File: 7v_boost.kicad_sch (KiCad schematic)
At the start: 5 parts, among them U401 LM27313XMFX/NOPB

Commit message: Update 7v_boost.kicad_sch
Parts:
- added C1401: 330pF 50V, BR_Passives:C_0402_1005Metric, symbol BR_Capacitors_0402:C_0402_330pF_50V_C0G_5%
- added R1401: 13.3k, BR_Passives:C_0402_1005Metric-minimized, symbol BR_Resistors_0402:R_0402_13k3
- added R1402: 62k, BR_Passives:C_0402_1005Metric-minimized, symbol BR_Resistors_0402:R_0402_62k
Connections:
- net GND: now also R1401.2
- net VIN: now reaches C402.1, L401.1, U401.4 (EN), U401.5 (VIN)
- net at D401.2 (A), L401.2, U401.1 (SW): now also C1401.1
- net VOUT: now reaches C401.1
- net VOUT: now also D401.1 (K), C1401.2, R1402.2
- net at U401.3 (FB): now also R1401.1, R1402.1
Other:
- note added: "Iout = 20mA deltaIL = Vin*tON/L = 9.42mA -> ILmax = 24.7mA < Isat"
- note added: "R1401 recommended to be 13.3k R1402 = R1401 * (Vout/1.23 - 1) = 62.3k"
- note added: "Vin = 4V Vout = 7V Vout = Vin/(1-D) -> D = 45.21% (including diode drop) -> tON = 283ns"
- moved on the sheet: C401, C402, D401, L401, U401

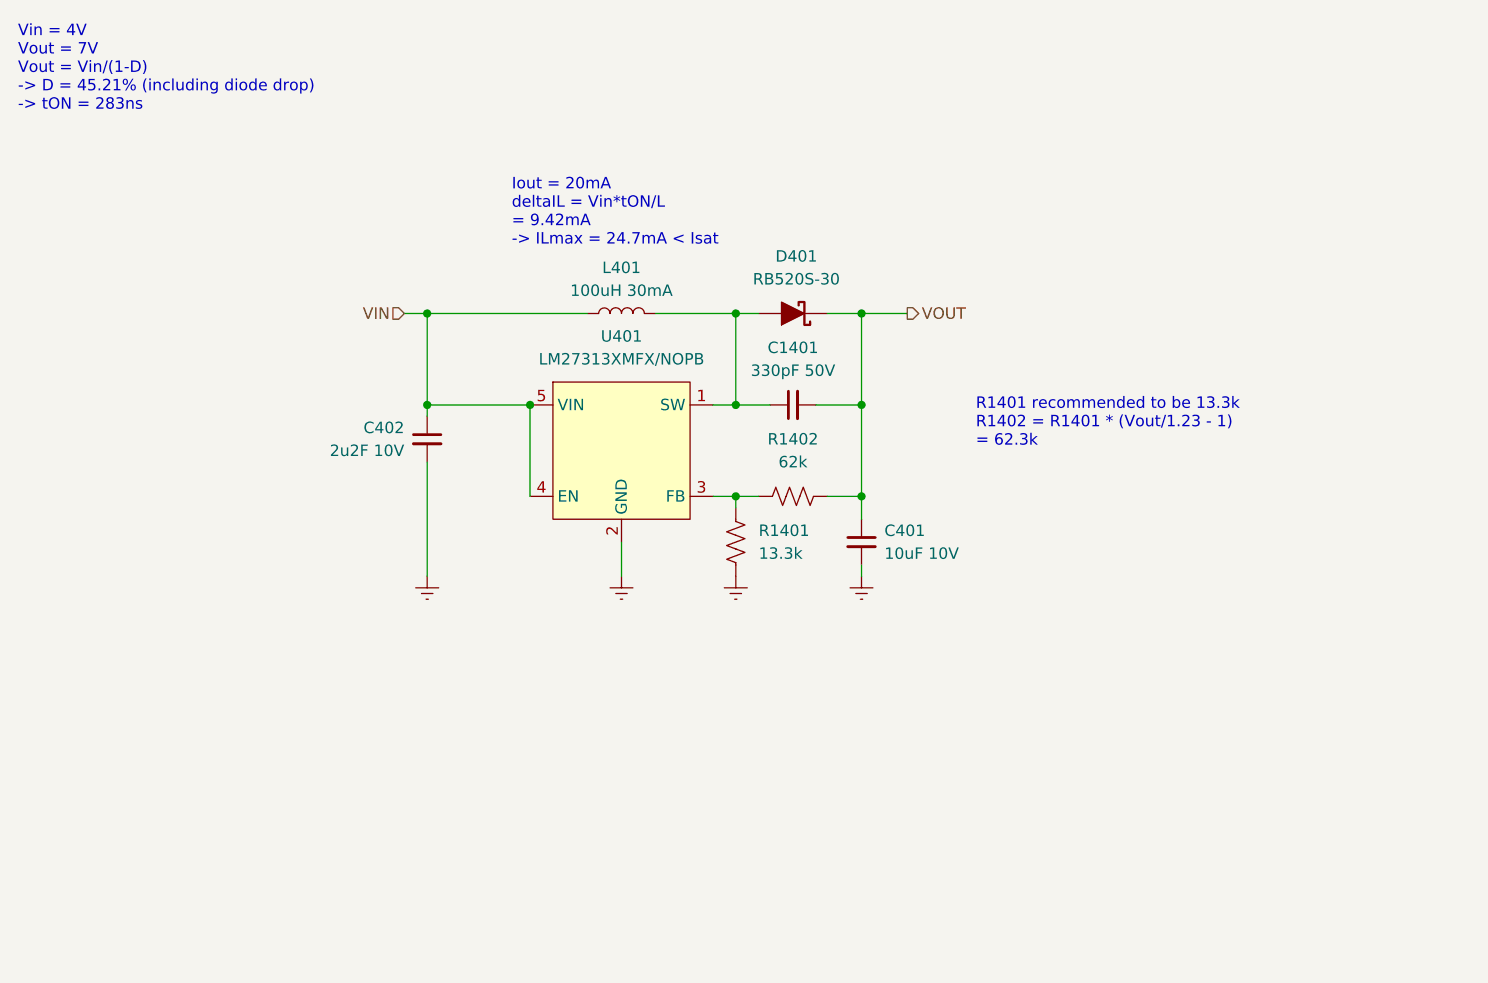
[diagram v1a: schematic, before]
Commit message: finished modifying vcc for sonar + 7V boost updates
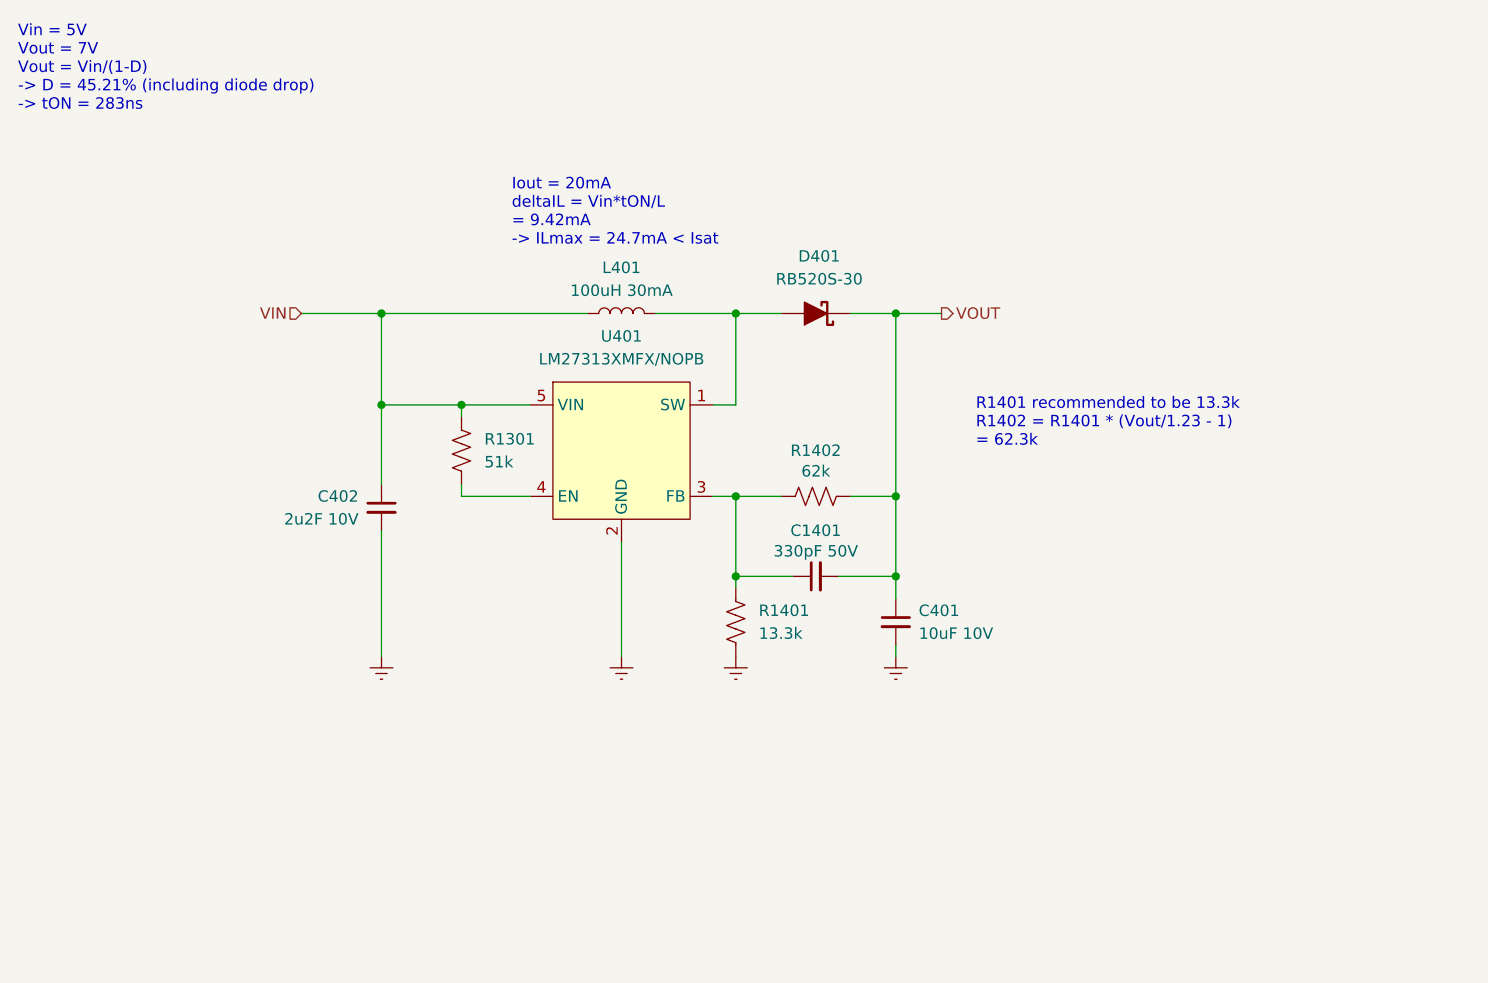
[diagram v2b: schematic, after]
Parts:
- added R1301: 51k, BR_Passives:C_0402_1005Metric-minimized, symbol BR_Resistors_0402:R_0402_51k
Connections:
- net VIN: now also R1301.1; no longer U401.4 (EN)
- net at D401.2 (A), L401.2, U401.1 (SW): no longer C1401.1
- net at R1401.1, R1402.1, U401.3 (FB): now also C1401.1
- new net: R1301.2, U401.4 (EN)
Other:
- note added: "Vin = 5V Vout = 7V Vout = Vin/(1-D) -> D = 45.21% (including diode drop) -> tON = 283ns"
- note removed: "Vin = 4V Vout = 7V Vout = Vin/(1-D) -> D = 45.21% (including diode drop) -> tON = 283ns"
- moved on the sheet: C1401, C401, C402, D401, R1401, R1402

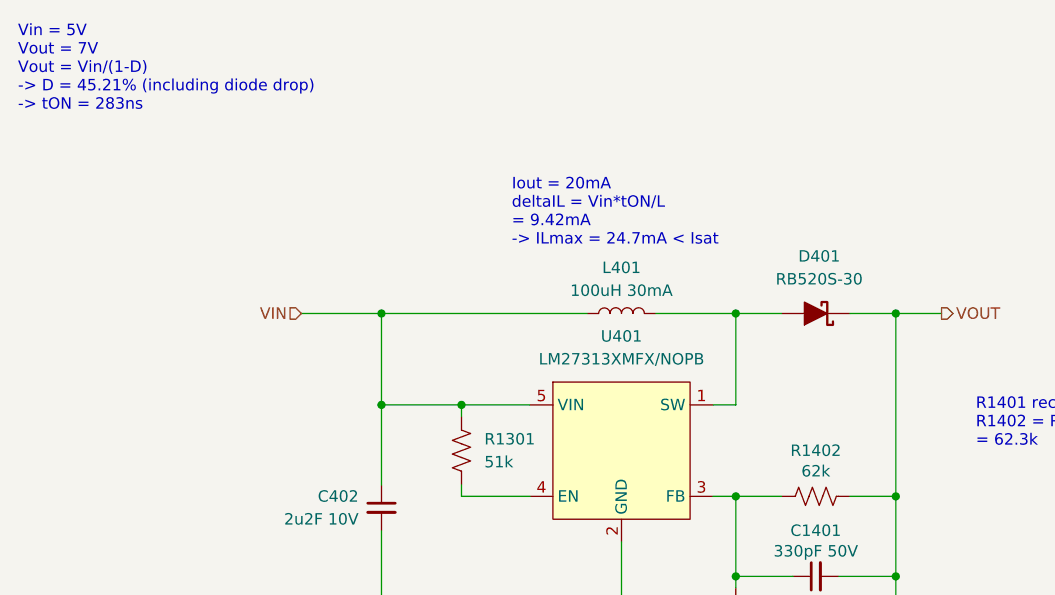
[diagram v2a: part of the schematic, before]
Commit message: implementing feedback + added stepper driver
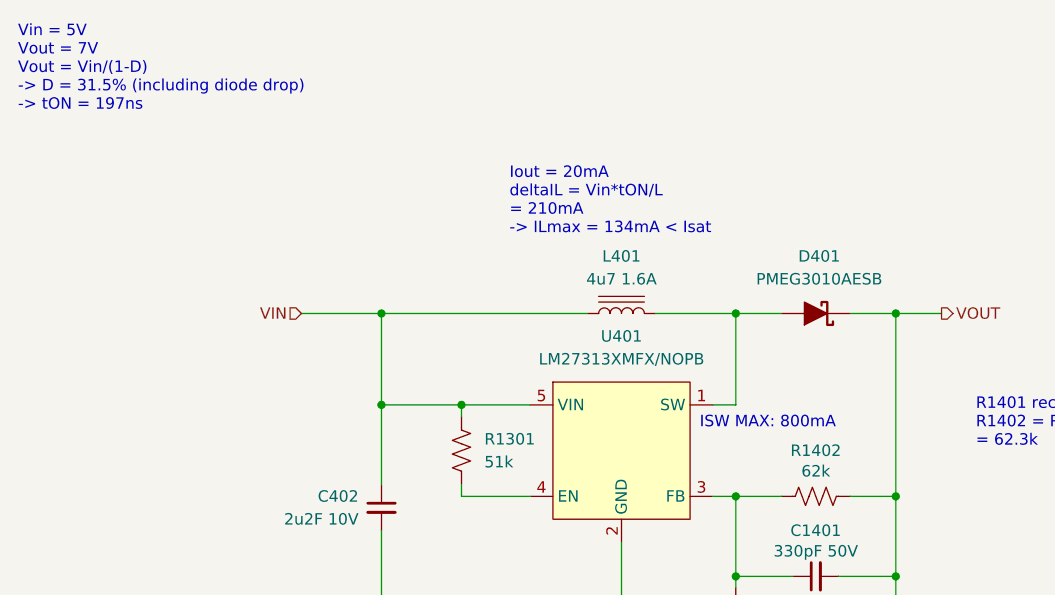
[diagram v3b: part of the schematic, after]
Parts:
- D401: value RB520S-30 -> PMEG3010AESB; footprint BR_Discretes:D_SOD-523 -> BR_Discretes:D_SOD-993-minimized; symbol BR_Diodes:D_Schottky_RB520S-30 -> BR_Diodes:D_Schottky_PMEG3010AESB; BRE Number BRE-000122 -> BRE-000120; JLCPCB Part Num C511880 -> C28646369; Manufacturer onsemi -> Nexperia; Manufacturer Part Num RB520S30T5G -> PMEG3010AESBYL; Supplier Part Num 1 RB520S30T5GOSCT-ND -> 1727-2401-2-ND; Supplier Part Num 2 863-RB520S30T5G -> 771-PMEG3010AESBYL; Supplier Part Num 3 C511880 -> C28646369
- L401: value 100uH 30mA -> 4u7 1.6A; footprint BR_Inductors:LMSC20120652R2MTA -> BR_Inductors:L_1008_2520Metric; symbol BR_Inductors:L_MLZ2012N101LT000 -> BR_Inductors:L_AWP_252012FW-4R7M; BRE Number BRE-001234 -> BRE-000220; JLCPCB Part Num C88184 -> C17225812; Manufacturer TDK -> TAI-TECH Advanced Electronics Co., Ltd.; Manufacturer Part Num MLZ2012N101LT000 -> AWP 252012FW-4R7M; Supplier 1 (none) -> DigiKey; Supplier 2 (none) -> DigiKey; Supplier 3 (none) -> JLCPCB; Supplier Part Num 1 (none) -> 4816-AWP252012FW-4R7MCT-ND; Supplier Part Num 2 (none) -> 4816-AWP252012FW-4R7MTR-ND; Supplier Part Num 3 (none) -> C17225812
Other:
- note added: "ISW MAX: 800mA"
- note added: "Iout = 20mA deltaIL = Vin*tON/L = 210mA -> ILmax = 134mA < Isat"
- note added: "Vin = 5V Vout = 7V Vout = Vin/(1-D) -> D = 31.5% (including diode drop) -> tON = 197ns"
- note removed: "Iout = 20mA deltaIL = Vin*tON/L = 9.42mA -> ILmax = 24.7mA < Isat"
- note removed: "Vin = 5V Vout = 7V Vout = Vin/(1-D) -> D = 45.21% (including diode drop) -> tON = 283ns"
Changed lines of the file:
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@@
 	(generator_version "9.0")
 	(paper "A5")
-	(text "Iout = 20mA\ndeltaIL = Vin*tON/L\n= 9.42mA\n-> ILmax = 24.7mA < Isat"
+	(text "ISW MAX: 800mA"
 		(exclude_from_sim no)
-		(at 83.058 38.354 0)
+		(at 111.506 61.722 0)
+		(effects
+			(font
+				(size 1.27 1.27)
+			)
+		)
+	)
+	(text "Iout = 20mA\ndeltaIL = Vin*tON/L\n= 210mA\n-> ILmax = 134mA < Isat"
+		(exclude_from_sim no)
+		(at 82.804 37.084 0)
 		(effects
 			(font
@@
 		)
 	)
-	(text "Vin = 5V\nVout = 7V\nVout = Vin/(1-D)\n-> D = 45.21% (including diode drop)\n-> tON = 283ns"
+	(text "Vin = 5V\nVout = 7V\nVout = Vin/(1-D)\n-> D = 31.5% (including diode drop)\n-> tON = 197ns"
 		(exclude_from_sim no)
 		(at 28.194 22.352 0)
@@
 	)
 	(symbol
-		(lib_id "BR_Inductors:L_MLZ2012N101LT000")
+		(lib_id "BR_Inductors:L_AWP_252012FW-4R7M")
 		(at 95.25 49.53 90)
 		(unit 1)
@@
 		(fields_autoplaced yes)
 		(property "Reference" "L401"
-			(at 95.25 44.45 90)
-			(effects
-				(font
-					(size 1.27 1.27)
-				)
-			)
-		)
-		(property "Value" "100uH 30mA"
-			(at 95.25 46.99 90)
-			(effects
-				(font
-					(size 1.27 1.27)
-				)
-			)
-		)
-		(property "Footprint" "BR_Inductors:LMSC20120652R2MTA"
+			(at 95.25 43.18 90)
+			(effects
+				(font
+					(size 1.27 1.27)
+				)
+			)
+		)
+		(property "Value" "4u7 1.6A"
+			(at 95.25 45.72 90)
+			(effects
+				(font
+					(size 1.27 1.27)
+				)
+			)
+		)
+		(property "Footprint" "BR_Inductors:L_1008_2520Metric"
 			(at 19.05 49.53 0)
 			(effects
@@
 			)
 		)
-		(property "Datasheet" "https://lcsc.com/datasheet/lcsc_datasheet_2412231059_TDK-MLZ2012N101LT000_C88184.pdf"
+		(property "Datasheet" "https://mm.digikey.com/Volume0/opasdata/d220001/medias/docus/5561/AWP%20Series.pdf"
 			(at 21.59 49.53 0)
 			(effects
@@
 			)
 		)
-		(property "Description" "100uH 20% 30mA 3.5Ω Inductors SMT 0805"
+		(property "Description" "4.7uH 20% 1.6A 175mR Shielded Molded Inductor SMT 1008 package"
 			(at 24.13 49.53 0)
 			(effects
@@
 			)
 		)
-		(property "Manufacturer" "TDK"
+		(property "Manufacturer" "TAI-TECH Advanced Electronics Co., Ltd."
 			(at 26.67 49.53 0)
 			(effects
@@
 			)
 		)
-		(property "Manufacturer Part Num" "MLZ2012N101LT000"
+		(property "Manufacturer Part Num" "AWP 252012FW-4R7M"
 			(at 29.21 49.53 0)
 			(effects
@@
 			)
 		)
-		(property "BRE Number" "BRE-001234"
+		(property "BRE Number" "BRE-000220"
 			(at 31.75 49.53 0)
 			(effects
@@
 			)
 		)
-		(property "JLCPCB Part Num" "C88184"
+		(property "JLCPCB Part Num" "C17225812"
+			(at 49.53 49.53 0)
+			(effects
+				(font
+					(size 1.27 1.27)
+				)
+				(justify left)
+				(hide yes)
+			)
+		)
+		(property "Supplier 1" "DigiKey"
 			(at 34.29 49.53 0)
+			(effects
+				(font
+					(size 1.27 1.27)
+				)
+				(justify left)
+				(hide yes)
+			)
+		)
+		(property "Supplier Part Num 1" "4816-AWP252012FW-4R7MCT-ND"
+			(at 36.83 49.53 0)
+			(effects
+				(font
+					(size 1.27 1.27)
+				)
+				(justify left)
+				(hide yes)
+			)
+		)
+		(property "Supplier 2" "DigiKey"
+			(at 39.37 49.53 0)
+			(effects
+				(font
+					(size 1.27 1.27)
+				)
+				(justify left)
+				(hide yes)
+			)
+		)
+		(property "Supplier Part Num 2" "4816-AWP252012FW-4R7MTR-ND"
+			(at 41.91 49.53 0)
+			(effects
+				(font
+					(size 1.27 1.27)
+				)
+				(justify left)
+				(hide yes)
+			)
+		)
+		(property "Supplier 3" "JLCPCB"
+			(at 44.45 49.53 0)
+			(effects
+				(font
+					(size 1.27 1.27)
+				)
+				(justify left)
+				(hide yes)
+			)
+		)
+		(property "Supplier Part Num 3" "C17225812"
+			(at 46.99 49.53 0)
 			(effects
 				(font
@@
 	)
 	(symbol
-		(lib_id "BR_Diodes:D_Schottky_RB520S-30")
+		(lib_id "BR_Diodes:D_Schottky_PMEG3010AESB")
 		(at 116.84 49.53 180)
 		(unit 1)
@@
 			)
 		)
-		(property "Value" "RB520S-30"
+		(property "Value" "PMEG3010AESB"
 			(at 117.221 45.72 0)
 			(effects
@@
 			)
 		)
-		(property "Footprint" "BR_Discretes:D_SOD-523"
+		(property "Footprint" "BR_Discretes:D_SOD-993-minimized"
 			(at 116.84 125.73 0)
 			(effects
@@
 			)
 		)
-		(property "Datasheet" "https://www.onsemi.com/pdf/datasheet/rb520s30t1-d.pdf"
+		(property "Datasheet" "https://assets.nexperia.com/documents/data-sheet/PMEG3010AESB.pdf"
 			(at 116.84 123.19 0)
 			(effects
@@
 			)
 		)
-		(property "Description" "Schottky Diode 30V 200mA SOD-523"
+		(property "Description" "Schottky Diode 30V 1A SOD-993"
+			(at 116.84 120.65 0)
+			(effects
+				(font
+					(size 1.27 1.27)
+				)
+				(justify left)
+				(hide yes)
+			)
+		)
+		(property "Manufacturer" "Nexperia"
+			(at 116.84 118.11 0)
+			(effects
+				(font
+					(size 1.27 1.27)
+				)
+				(justify left)
+				(hide yes)
+			)
+		)
+		(property "Manufacturer Part Num" "PMEG3010AESBYL"
+			(at 116.84 115.57 0)
+			(effects
+				(font
+					(size 1.27 1.27)
+				)
+				(justify left)
+				(hide yes)
+			)
+		)
+		(property "BRE Number" "BRE-000120"
 			(at 116.84 113.03 0)
-			(effects
-				(font
-					(size 1.27 1.27)
-				)
-				(justify left)
-				(hide yes)
-			)
-		)
-		(property "Manufacturer" "onsemi"
-			(at 116.84 120.65 0)
-			(effects
-				(font
-					(size 1.27 1.27)
-				)
-				(justify left)
-				(hide yes)
-			)
-		)
-		(property "Manufacturer Part Num" "RB520S30T5G"
-			(at 116.84 118.11 0)
-			(effects
-				(font
-					(size 1.27 1.27)
-				)
-				(justify left)
-				(hide yes)
-			)
-		)
-		(property "BRE Number" "BRE-000122"
-			(at 116.84 115.57 0)
 			(effects
 				(font
@@
 			)
 		)
-		(property "Supplier Part Num 1" "RB520S30T5GOSCT-ND"
+		(property "Supplier Part Num 1" "1727-2401-2-ND"
 			(at 116.84 107.95 0)
 			(effects
@@
 			)
 		)
-		(property "Supplier Part Num 2" "863-RB520S30T5G"
+		(property "Supplier Part Num 2" "771-PMEG3010AESBYL"
 			(at 116.84 102.87 0)
 			(effects
@@
 			)
 		)
-		(property "Supplier Part Num 3" "C511880"
+		(property "Supplier Part Num 3" "C28646369"
 			(at 116.84 97.79 0)
 			(effects
@@
 			)
 		)
-		(property "JLCPCB Part Num" "C511880"
-			(at 116.84 90.17 0)
-			(effects
-				(font
+		(property "JLCPCB Part Num" "C28646369"
+			(at 116.84 95.25 0)
+			(effects
+				(font

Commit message: completed feedback from review + reannotated sheets
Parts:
- renumbered C402 to C1301, C1401 to C1302, C401 to C1303, D401 to D1301, L401 to L1301, R1401 to R1302, R1402 to R1303, U401 to U1301
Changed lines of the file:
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@@
 		(dnp no)
 		(fields_autoplaced yes)
-		(property "Reference" "#PWR0403"
+		(property "Reference" "#PWR01302"
 			(at 95.25 93.98 0)
 			(effects
@@
 			(project "SonarDevBoard"
 				(path "/2a5ce3ef-537a-4122-a1be-ef76186bc0d7/774f2c6c-c15c-4713-acf0-4edb2ec6be20/ba770378-fa99-4e9b-ba3e-dcadec87fa26"
-					(reference "#PWR0403")
+					(reference "#PWR01302")
 					(unit 1)
 				)
@@
 		(on_board yes)
 		(dnp no)
-		(property "Reference" "C1401"
+		(property "Reference" "C1302"
 			(at 116.84 73.66 90)
 			(effects
@@
 			(project ""
 				(path "/2a5ce3ef-537a-4122-a1be-ef76186bc0d7/774f2c6c-c15c-4713-acf0-4edb2ec6be20/ba770378-fa99-4e9b-ba3e-dcadec87fa26"
-					(reference "C1401")
+					(reference "C1302")
 					(unit 1)
 				)
@@
 		(on_board yes)
 		(dnp no)
-		(property "Reference" "C402"
+		(property "Reference" "C1301"
 			(at 66.04 69.8562 0)
 			(effects
@@
 			(project "SonarDevBoard"
 				(path "/2a5ce3ef-537a-4122-a1be-ef76186bc0d7/774f2c6c-c15c-4713-acf0-4edb2ec6be20/ba770378-fa99-4e9b-ba3e-dcadec87fa26"
-					(reference "C402")
+					(reference "C1301")
 					(unit 1)
 				)
@@
 		(dnp no)
 		(fields_autoplaced yes)
-		(property "Reference" "L401"
+		(property "Reference" "L1301"
 			(at 95.25 43.18 90)
 			(effects
@@
 			(project "SonarDevBoard"
 				(path "/2a5ce3ef-537a-4122-a1be-ef76186bc0d7/774f2c6c-c15c-4713-acf0-4edb2ec6be20/ba770378-fa99-4e9b-ba3e-dcadec87fa26"
-					(reference "L401")
+					(reference "L1301")
 					(unit 1)
 				)
@@
 		(dnp no)
 		(fields_autoplaced yes)
-		(property "Reference" "R1401"
+		(property "Reference" "R1302"
 			(at 110.49 82.5499 0)
 			(effects
@@
 			(project ""
 				(path "/2a5ce3ef-537a-4122-a1be-ef76186bc0d7/774f2c6c-c15c-4713-acf0-4edb2ec6be20/ba770378-fa99-4e9b-ba3e-dcadec87fa26"
-					(reference "R1401")
+					(reference "R1302")
 					(unit 1)
 				)
@@
 		(dnp no)
 		(fields_autoplaced yes)
-		(property "Reference" "#PWR01401"
+		(property "Reference" "#PWR01303"
 			(at 107.95 93.98 0)
 			(effects
@@
 			(project "SonarDevBoard"
 				(path "/2a5ce3ef-537a-4122-a1be-ef76186bc0d7/774f2c6c-c15c-4713-acf0-4edb2ec6be20/ba770378-fa99-4e9b-ba3e-dcadec87fa26"
-					(reference "#PWR01401")
+					(reference "#PWR01303")
 					(unit 1)
 				)
@@
 		(dnp no)
 		(fields_autoplaced yes)
-		(property "Reference" "C401"
+		(property "Reference" "C1303"
 			(at 128.27 82.5562 0)
 			(effects
@@
 			(project "SonarDevBoard"
 				(path "/2a5ce3ef-537a-4122-a1be-ef76186bc0d7/774f2c6c-c15c-4713-acf0-4edb2ec6be20/ba770378-fa99-4e9b-ba3e-dcadec87fa26"
-					(reference "C401")
+					(reference "C1303")
 					(unit 1)
 				)
@@
 		(dnp no)
 		(fields_autoplaced yes)
-		(property "Reference" "D401"
+		(property "Reference" "D1301"
 			(at 117.221 43.18 0)
 			(effects
@@
 			(project "SonarDevBoard"
 				(path "/2a5ce3ef-537a-4122-a1be-ef76186bc0d7/774f2c6c-c15c-4713-acf0-4edb2ec6be20/ba770378-fa99-4e9b-ba3e-dcadec87fa26"
-					(reference "D401")
+					(reference "D1301")
 					(unit 1)
 				)
@@
 		(on_board yes)
 		(dnp no)
-		(property "Reference" "R1402"
+		(property "Reference" "R1303"
 			(at 116.84 64.77 90)
 			(effects
@@
 			(project ""
 				(path "/2a5ce3ef-537a-4122-a1be-ef76186bc0d7/774f2c6c-c15c-4713-acf0-4edb2ec6be20/ba770378-fa99-4e9b-ba3e-dcadec87fa26"
-					(reference "R1402")
+					(reference "R1303")
 					(unit 1)
 				)
@@
 		(dnp no)
 		(fields_autoplaced yes)
-		(property "Reference" "#PWR0402"
+		(property "Reference" "#PWR01304"
 			(at 125.73 93.98 0)
 			(effects
@@
 			(project "SonarDevBoard"
 				(path "/2a5ce3ef-537a-4122-a1be-ef76186bc0d7/774f2c6c-c15c-4713-acf0-4edb2ec6be20/ba770378-fa99-4e9b-ba3e-dcadec87fa26"
-					(reference "#PWR0402")
+					(reference "#PWR01304")
 					(unit 1)
 				)
@@
 		(dnp no)
 		(fields_autoplaced yes)
-		(property "Reference" "#PWR0401"
+		(property "Reference" "#PWR01301"
 			(at 68.58 93.98 0)
 			(effects
@@
 			(project "SonarDevBoard"
 				(path "/2a5ce3ef-537a-4122-a1be-ef76186bc0d7/774f2c6c-c15c-4713-acf0-4edb2ec6be20/ba770378-fa99-4e9b-ba3e-dcadec87fa26"
-					(reference "#PWR0401")
+					(reference "#PWR01301")
 					(unit 1)
 				)
@@
 		(dnp no)
 		(fields_autoplaced yes)
-		(property "Reference" "U401"
+		(property "Reference" "U1301"
 			(at 95.25 52.07 0)
 			(effects
@@
 			(project "SonarDevBoard"
 				(path "/2a5ce3ef-537a-4122-a1be-ef76186bc0d7/774f2c6c-c15c-4713-acf0-4edb2ec6be20/ba770378-fa99-4e9b-ba3e-dcadec87fa26"
-					(reference "U401")
+					(reference "U1301")
 					(unit 1)
 				)
